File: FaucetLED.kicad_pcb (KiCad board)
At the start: 2 copper layers, 34.5 x 28.4 mm, 41 parts, among them P1 CONN_01X03, P2 CONN_01X02, P4 CONN_01X03, P5 CONN_01X02, P6 CONN_01X01, Q1 BSS138, Q2 BSS138, Q3 BSS138, U1 TLV70033DDC, U2 STM32L052KxTx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

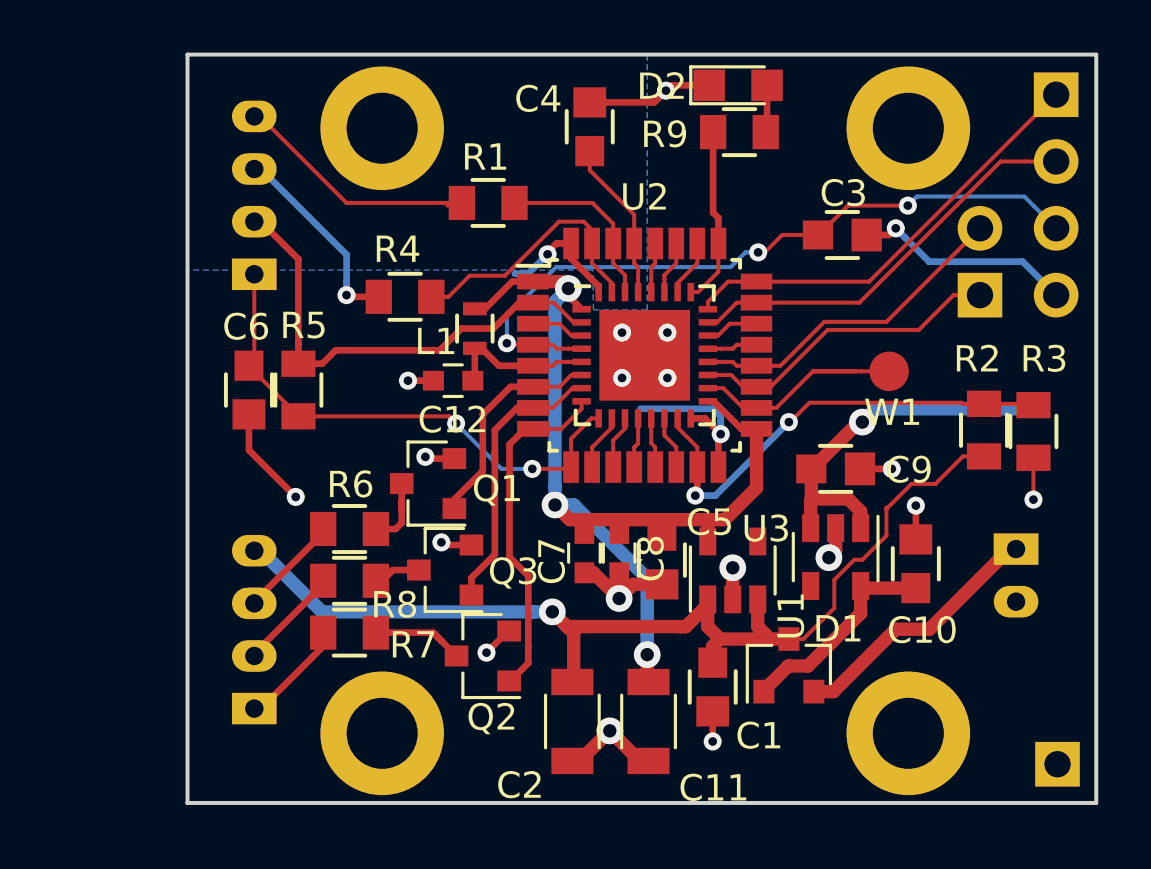
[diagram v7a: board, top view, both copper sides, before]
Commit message: Restore accidentally deleted battery holder.
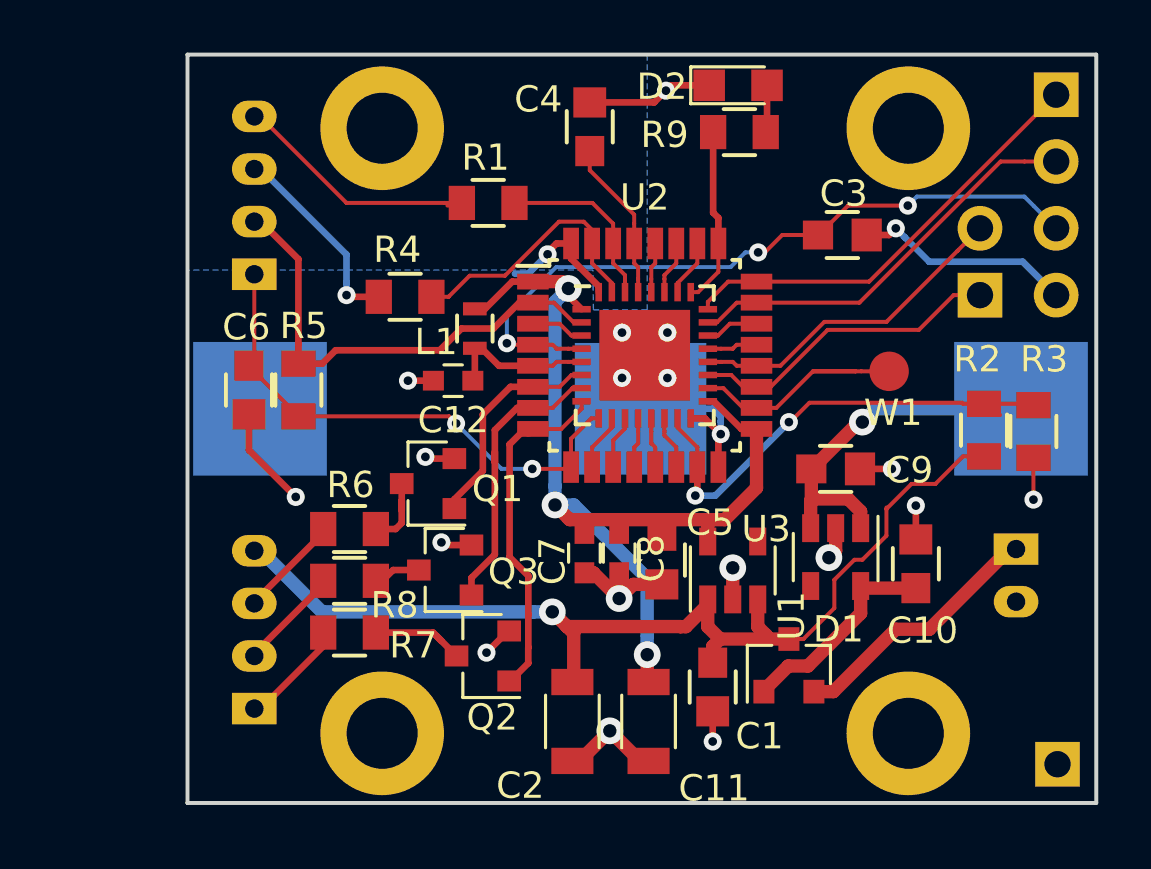
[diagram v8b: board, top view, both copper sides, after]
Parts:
- added BT1: CR2016x2, components:Keystone_3020_2x2016-CoinCell, B.Cu at (118.8, 89.7)
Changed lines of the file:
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@@
 (kicad_pcb (version 4) (host pcbnew 4.0.5)
   (general
-    (links 110)
+    (links 112)
     (no_connects 0)
-    (area 101.524999 76.124999 136.219001 104.723001)
+    (area 93.919029 74.7226 144.080972 109.11562)
     (thickness 1.6)
     (drawings 5)
     (tracks 446)
     (zones 0)
-    (modules 41)
+    (modules 42)
     (nets 43)
   )
@@
   )
   (setup
-    (last_trace_width 0.508)
+    (last_trace_width 0.254)
     (user_trace_width 0.1524)
     (user_trace_width 0.254)
@@
     )
   )
+  (module components:Keystone_3020_2x2016-CoinCell locked (layer B.Cu)
+    (at 118.8212 89.662 180)
+    (descr http://www.keyelco.com/product-pdf.cfm?p=14028)
+    (tags "Keystone type 1058 coin cell retainer")
+    (attr smd)
+    (fp_text reference BT1 (at 0 -7.62 180) (layer B.SilkS)
+      (effects (font (size 1 1) (thickness 0.15)) (justify mirror))
+    )
+    (fp_text value CR2016x2 (at 0 9.398 180) (layer B.Fab)
+      (effects (font (size 1 1) (thickness 0.15)) (justify mirror))
+    )
+    (fp_arc (start 0 0) (end 11.06 -4.11) (angle -139.2) (layer B.CrtYd) (width 0.05))
+    (fp_arc (start 0 0) (end -11.06 4.11) (angle -139.2) (layer B.CrtYd) (width 0.05))
+    (fp_line (start 11.06 -4.11) (end 16.45 -4.11) (layer B.CrtYd) (width 0.05))
+    (fp_line (start 16.45 -4.11) (end 16.45 4.11) (layer B.CrtYd) (width 0.05))
+    (fp_line (start 16.45 4.11) (end 11.06 4.11) (layer B.CrtYd) (width 0.05))
+    (fp_line (start -16.45 4.11) (end -11.06 4.11) (layer B.CrtYd) (width 0.05))
+    (fp_line (start -16.45 4.11) (end -16.45 -4.11) (layer B.CrtYd) (width 0.05))
+    (fp_line (start -16.45 -4.11) (end -11.06 -4.11) (layer B.CrtYd) (width 0.05))
+    (fp_arc (start 0 0) (end -10.692 -3.61) (angle 27.3) (layer B.SilkS) (width 0.12))
+    (fp_arc (start 0 0) (end 10.692 3.61) (angle 27.3) (layer B.SilkS) (width 0.12))
+    (fp_arc (start 0 0) (end 10.692 -3.61) (angle -27.3) (layer B.SilkS) (width 0.12))
+    (fp_arc (start 0 0) (end -10.692 3.61) (angle -27.3) (layer B.SilkS) (width 0.12))
+    (fp_line (start -14.3 -2.8) (end -14.31 -3.61) (layer B.SilkS) (width 0.12))
+    (fp_line (start -10.692 -3.61) (end -14.31 -3.61) (layer B.SilkS) (width 0.12))
+    (fp_line (start -3.86 -8.11) (end -7.8473 -8.11) (layer B.SilkS) (width 0.12))
+    (fp_line (start -1.66 -5.91) (end -3.86 -8.11) (layer B.SilkS) (width 0.12))
+    (fp_line (start 1.66 -5.91) (end -1.66 -5.91) (layer B.SilkS) (width 0.12))
+    (fp_line (start 1.66 -5.91) (end 3.86 -8.11) (layer B.SilkS) (width 0.12))
+    (fp_line (start 7.8473 -8.11) (end 3.86 -8.11) (layer B.SilkS) (width 0.12))
+    (fp_line (start 14.3 -2.8) (end 14.31 -3.61) (layer B.SilkS) (width 0.12))
+    (fp_line (start 14.31 -3.61) (end 10.692 -3.61) (layer B.SilkS) (width 0.12))
+    (fp_line (start 10.692 3.61) (end 14.31 3.61) (layer B.SilkS) (width 0.12))
+    (fp_line (start 14.3 2.8) (end 14.31 3.61) (layer B.SilkS) (width 0.12))
+    (fp_line (start -7.8473 8.11) (end 7.8473 8.11) (layer B.SilkS) (width 0.12))
+    (fp_line (start -14.3 2.6) (end -14.31 3.61) (layer B.SilkS) (width 0.12))
+    (fp_line (start -14.31 3.61) (end -10.692 3.61) (layer B.SilkS) (width 0.12))
+    (fp_arc (start 0 0) (end -10.61275 -3.5) (angle 27.4635) (layer B.Fab) (width 0.1))
+    (fp_arc (start 0 0) (end 10.61275 3.5) (angle 27.4635) (layer B.Fab) (width 0.1))
+    (fp_arc (start 0 0) (end 10.61275 -3.5) (angle -27.4635) (layer B.Fab) (width 0.1))
+    (fp_line (start 14.2 -2.8) (end 14.2 -3.5) (layer B.Fab) (width 0.1))
+    (fp_line (start 14.2 -3.5) (end 10.61275 -3.5) (layer B.Fab) (width 0.1))
+    (fp_line (start 10.61275 3.5) (end 14.2 3.5) (layer B.Fab) (width 0.1))
+    (fp_line (start 14.2 3.5) (end 14.2 2.8) (layer B.Fab) (width 0.1))
+    (fp_line (start -14.2 -2.8) (end -14.2 -3.5) (layer B.Fab) (width 0.1))
+    (fp_line (start -14.2 -3.5) (end -10.61275 -3.5) (layer B.Fab) (width 0.1))
+    (fp_line (start 3.9 -8) (end 7.8026 -8) (layer B.Fab) (width 0.1))
+    (fp_line (start 1.7 -5.8) (end 3.9 -8) (layer B.Fab) (width 0.1))
+    (fp_line (start -1.7 -5.8) (end -3.9 -8) (layer B.Fab) (width 0.1))
+    (fp_line (start -1.7 -5.8) (end 1.7 -5.8) (layer B.Fab) (width 0.1))
+    (fp_line (start -14.2 3.5) (end -10.61275 3.5) (layer B.Fab) (width 0.1))
+    (fp_line (start -14.2 3.5) (end -14.2 2.6) (layer B.Fab) (width 0.1))
+    (fp_line (start -3.9 -8) (end -7.8026 -8) (layer B.Fab) (width 0.1))
+    (fp_line (start -7.8026 8) (end 7.8026 8) (layer B.Fab) (width 0.1))
+    (fp_arc (start 0 0) (end -10.61275 3.5) (angle -27.4635) (layer B.Fab) (width 0.1))
+    (fp_circle (center 0 0) (end 10 0) (layer Dwgs.User) (width 0.15))
+    (pad 1 smd rect (at -14.465 0 180) (size 5.08 5.08) (layers B.Cu B.Paste B.Mask)
+      (net 19 "Net-(BT1-Pad1)"))
+    (pad 3 smd rect (at 14.465 0 180) (size 5.08 5.08) (layers B.Cu B.Paste B.Mask))
+    (pad 2 smd rect (at 0 0 180) (size 5 5) (layers B.Cu B.Paste B.Mask)
+      (net 1 GND))
+  )
   (module components:LQFP-32_7x7mm_Pitch0.8mm_QFN-32-1EP_5x5mm_Pitch0.5mm-Combo locked (layer F.Cu)
